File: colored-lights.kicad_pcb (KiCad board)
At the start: 2 copper layers, 162.6 x 99.1 mm, 65 parts, among them J1 Conn_01x06, J10 Conn_01x06, J11 24V, J12 24V, J13 SIGNAL, J14 GND, J15 GND, J16 Conn_01x06, J17 Conn_01x06, J2 Conn_01x06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

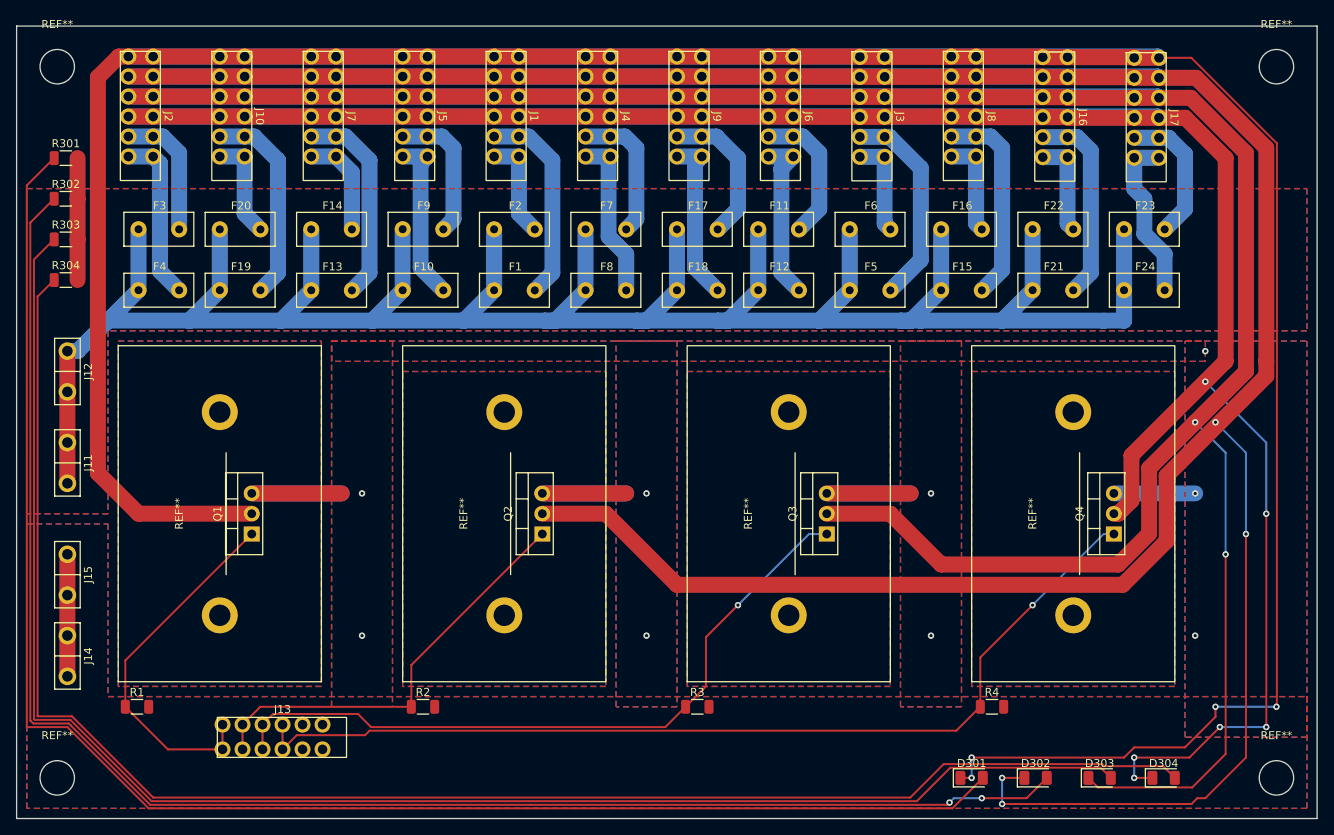
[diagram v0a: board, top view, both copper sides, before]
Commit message: finish p1 board layout
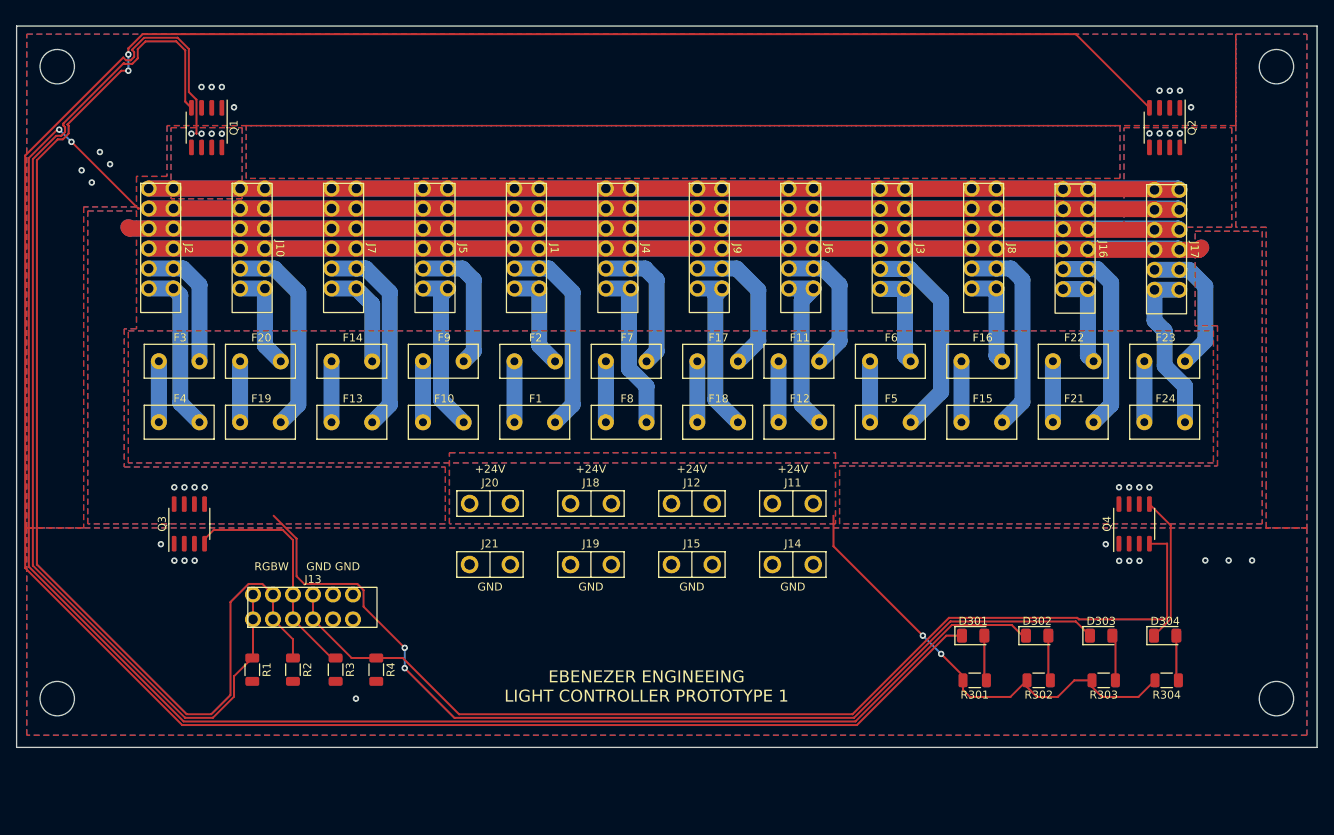
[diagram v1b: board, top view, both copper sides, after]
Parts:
- removed REF** (x4): 6400BG, Library:6400BG
- removed REF**: MountingHole_4.3mm_M4, MountingHole:MountingHole_4.3mm_M4
- added  : , MountingHole:MountingHole_4.3mm_M4, F.Cu at (72.4, 123.4)
- added J18: 24V, Library:1212, F.Cu at (139.1, 99.1)
- added J19: GND, Library:1212, F.Cu at (139.1, 106.7)
- added J20: 24V, Library:1212, F.Cu at (126.5, 99.1)
- added J21: GND, Library:1212, F.Cu at (126.5, 106.7)
-  : renamed from REF**; value MountingHole_4.3mm_M4 -> (none) (x3)
- Q1, Q2, Q3, Q4: value FQP30N06L-ND -> Si4122DY; footprint Package_TO_SOT_THT:TO-220-3_Vertical -> Library:SOIC-8_3.9x4.9mm_P1.27mm transistor
- moved R304 146.4 mm to (211.1, 121.2), turned to 180 degrees
- moved R303 141.0 mm to (203.2, 121.2), turned to 180 degrees
- moved R302 135.7 mm to (195.1, 121.2), turned to 180 degrees
- moved R301 131.0 mm to (187.1, 121.2), turned to 180 degrees
- moved Q2 92.9 mm to (210.8, 52.1), turned to -90 degrees
- moved J14 91.4 mm to (164.3, 106.7), turned to 180 degrees
- moved J11 90.8 mm to (164.3, 99.1), turned to 180 degrees
- moved J12 79.8 mm to (151.7, 99.1), turned to 180 degrees
- moved Q3 79.7 mm to (88.9, 101.6)
- moved J15 78.1 mm to (151.7, 106.7), turned to 180 degrees
- moved R4 77.1 mm to (112.3, 119.8), turned to -90 degrees
- moved Q1 51.1 mm to (91.1, 52.1), turned to -90 degrees
- moved R3 45.4 mm to (107.2, 119.8), turned to -90 degrees
- moved D301 17.8 mm to (186.9, 115.6)
- moved D302 17.8 mm to (194.9, 115.6)
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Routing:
- net GREEN_INPUT: track 53.5 -> 262.9 mm, vias 0 -> 2
- net Net-(D304-Pad2): track 204.2 -> 5.69 mm
- net Net-(D303-Pad2): track 202.1 -> 5.75 mm
- net Net-(D302-Pad2): track 199.3 -> 5.69 mm, vias 2 -> 0
- net Net-(D301-Pad2): track 197.8 -> 5.69 mm
- net 24V: track 325.0 -> 149.5 mm, vias 0 -> 2
- net WHITE_OUTPUT: track 388.0 -> 282.0 mm, vias 6 -> 4
- net GND: track 89.9 -> 0.00 mm, vias 9 -> 24
- net RED_INPUT: track 46.0 -> 133.5 mm
- net BLUE_INPUT: track 88.5 -> 29.9 mm, vias 1 -> 0
- net BLUE_OUTPUT: track 431.1 -> 386.7 mm, vias 2 -> 6
- net GREEN_OUTPUT: track 495.6 -> 467.6 mm, vias 4 -> 6
- net RED_OUTPUT: track 468.5 -> 478.6 mm
- net WHITE_INPUT: track 121.8 -> 131.4 mm, vias 1 -> 0
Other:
- board size 162.6 x 99.1 mm -> 162.6 x 90.2 mm
- board text added: "+24V"
- board text added: "EBENEZER ENGINEEING LIGHT CONTROLLER PROTOTYPE 1"
- board text added: "GND"
- board text added: "RGBW GND GND"

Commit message: Adjusted indicator LEDs * Increased value to decrease brightness and power usage * Increased size to handle heat and make assembly easier
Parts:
- R301, R302, R303, R304: value 1k -> 2k; footprint Resistor_SMD:R_1206_3216Metric -> Resistor_SMD:R_2010_5025Metric
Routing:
- net 24V: track 149.5 -> 147.9 mm

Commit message: Silkscreen updates & improvements
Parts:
- added G***: LOGO, Library:ebenezer_logo, F.Cu at (86.4, 121.3)
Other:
- board text added: "EBEN-EZER ENGINEEING"
- board text added: "LIGHT CONTROLLER V2"
- board text added: "POWER INPUT"
- board text added: "RED - GREEN - BLUE - WHITE - 900mA + 900mA +"
- board text added: "RED GREEN BLUE WHITE GND GND"
- board text added: "SIGNAL +5V"
- board text removed: "EBENEZER ENGINEEING LIGHT CONTROLLER PROTOTYPE 1"
- board text removed: "RGBW GND GND"

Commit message: corrected typo
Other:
- board text added: "EBEN-EZER ENGINEERING"
- board text removed: "EBEN-EZER ENGINEEING"
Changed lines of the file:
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@@
     (effects (font (size 1 1) (thickness 0.15)))
   )
-  (gr_text "EBEN-EZER ENGINEEING" (at 90.805 125.095) (layer "F.SilkS")
+  (gr_text "EBEN-EZER ENGINEERING" (at 90.805 125.095) (layer "F.SilkS")
     (effects (font (size 2 2) (thickness 0.3)) (justify left))
   )
